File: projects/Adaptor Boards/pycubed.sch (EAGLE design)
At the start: 13 parts, among them J1 M22-6013005

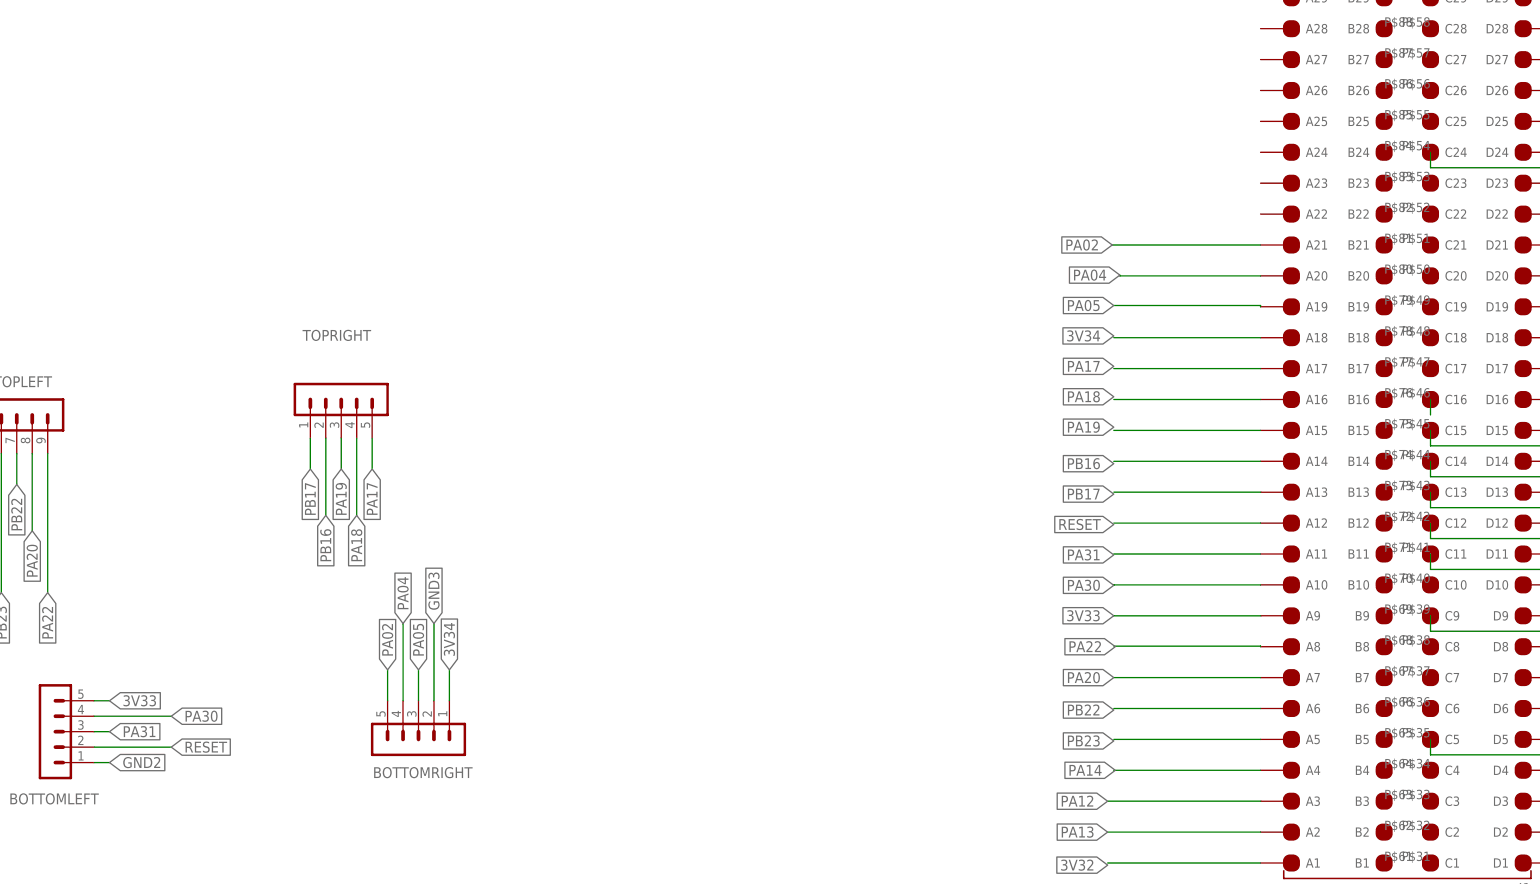
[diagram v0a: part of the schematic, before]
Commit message: Updated PCB desgins to fix wiring mismatches
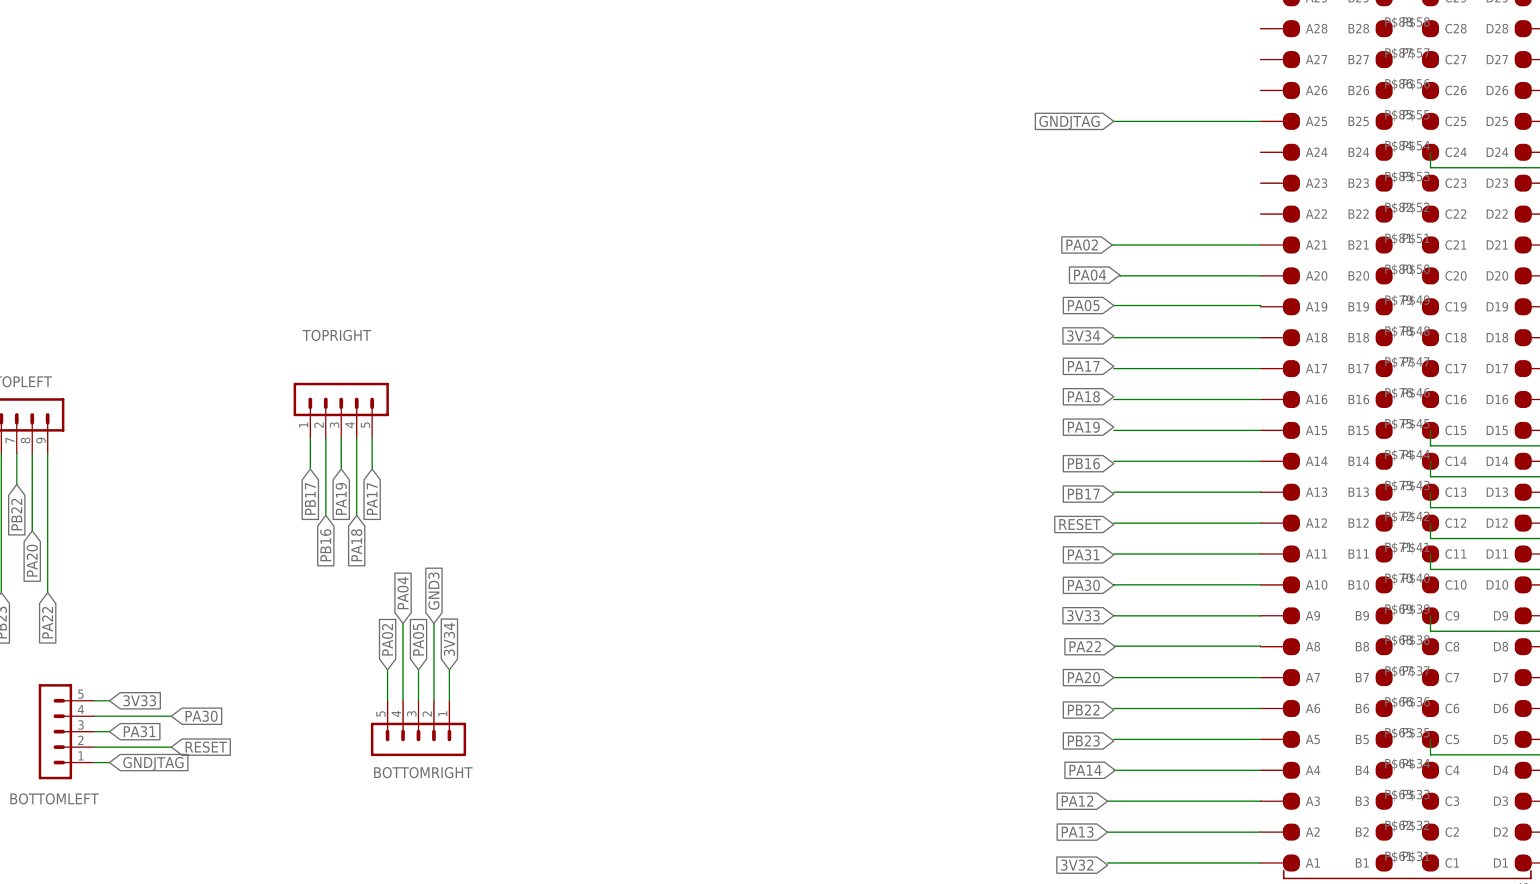
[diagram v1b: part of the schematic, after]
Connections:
- new net GNDJTAG: BOTTOMLEFT.1, J1.A25
- net GND2: no longer BOTTOMLEFT.1
- net GND8: no longer J1.C16
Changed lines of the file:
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@@
 <label x="205.74" y="36.83" size="1.778" layer="95" xref="yes"/>
-</segment>
-<segment>
-<pinref part="BOTTOMLEFT" gate="G$1" pin="1"/>
-<wire x1="-40.64" y1="22.86" x2="-38.1" y2="22.86" width="0.1524" layer="91"/>
-<label x="-38.1" y="22.86" size="1.778" layer="95" xref="yes"/>
 </segment>
 </net>
@@
 <net name="GND8" class="0">
 <segment>
-<pinref part="J1" gate="G$1" pin="C16"/>
-<wire x1="179.07" y1="82.55" x2="179.07" y2="80.01" width="0.1524" layer="91"/>
-</segment>
-<segment>
 <pinref part="J1" gate="G$1" pin="D16"/>
 <wire x1="199.39" y1="82.55" x2="207.01" y2="82.55" width="0.1524" layer="91"/>
@@
 </segment>
 </net>
+<net name="GNDJTAG" class="0">
+<segment>
+<pinref part="BOTTOMLEFT" gate="G$1" pin="1"/>
+<wire x1="-40.64" y1="22.86" x2="-38.1" y2="22.86" width="0.1524" layer="91"/>
+<label x="-38.1" y="22.86" size="1.778" layer="95" xref="yes"/>
+</segment>
+<segment>
+<pinref part="J1" gate="G$1" pin="A25"/>
+<wire x1="151.13" y1="128.27" x2="127" y2="128.27" width="0.1524" layer="91"/>
+<label x="127" y="128.27" size="1.778" layer="95" rot="R180" xref="yes"/>
+</segment>
+</net>
